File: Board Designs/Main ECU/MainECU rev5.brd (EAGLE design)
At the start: 120.6 x 78.9 mm, 164 parts, among them Q10 MMBT3904LT3G, Q11 MMBT3904LT3G, Q9 MMBT3904LT3G, X1 CONNECTOR-37, X2 CONNECTOR-4AUTOSPORT, X3 CONNECTOR-4NANO-FIT-VERTICAL-4, X4 CONNECTOR-4NANO-FIT-VERTICAL-4

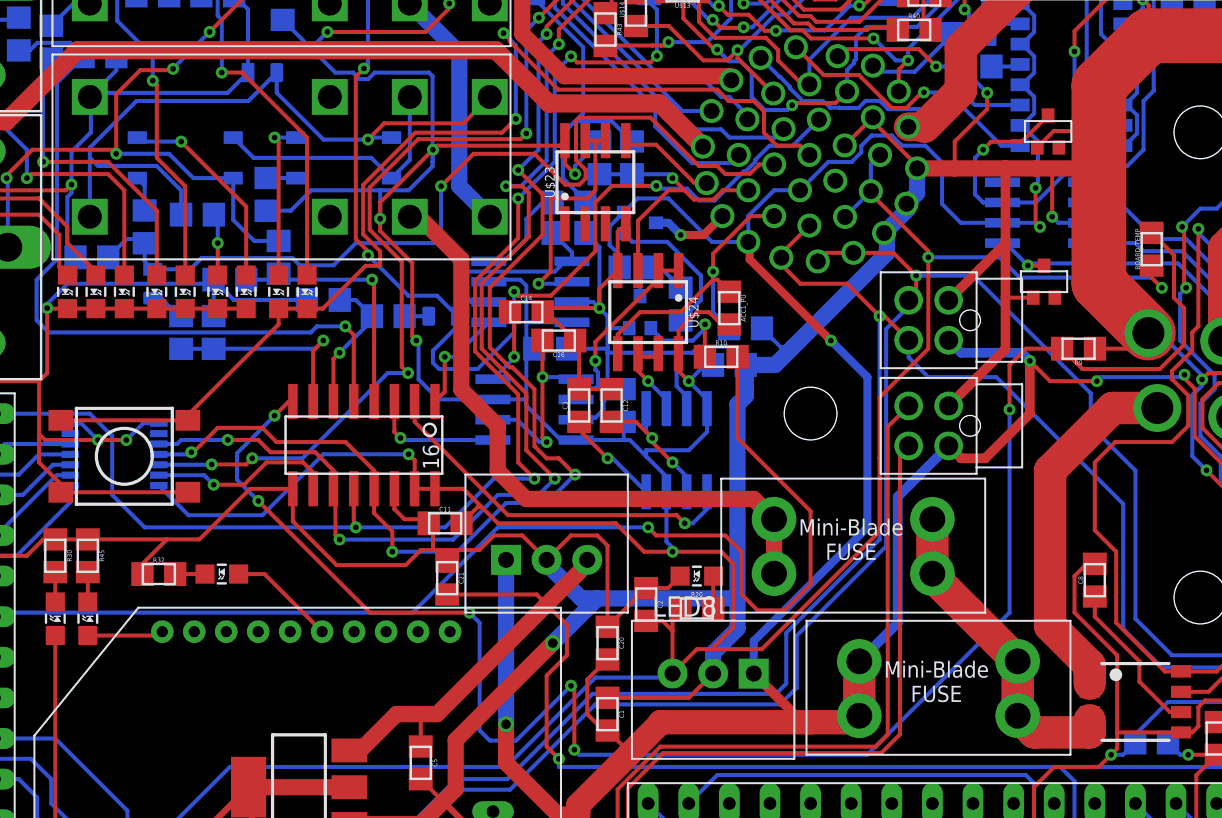
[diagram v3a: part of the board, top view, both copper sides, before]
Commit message: MainECU rev5: Added current sensor filter caps, fixed level shifter OE pin, various tweaks to traces
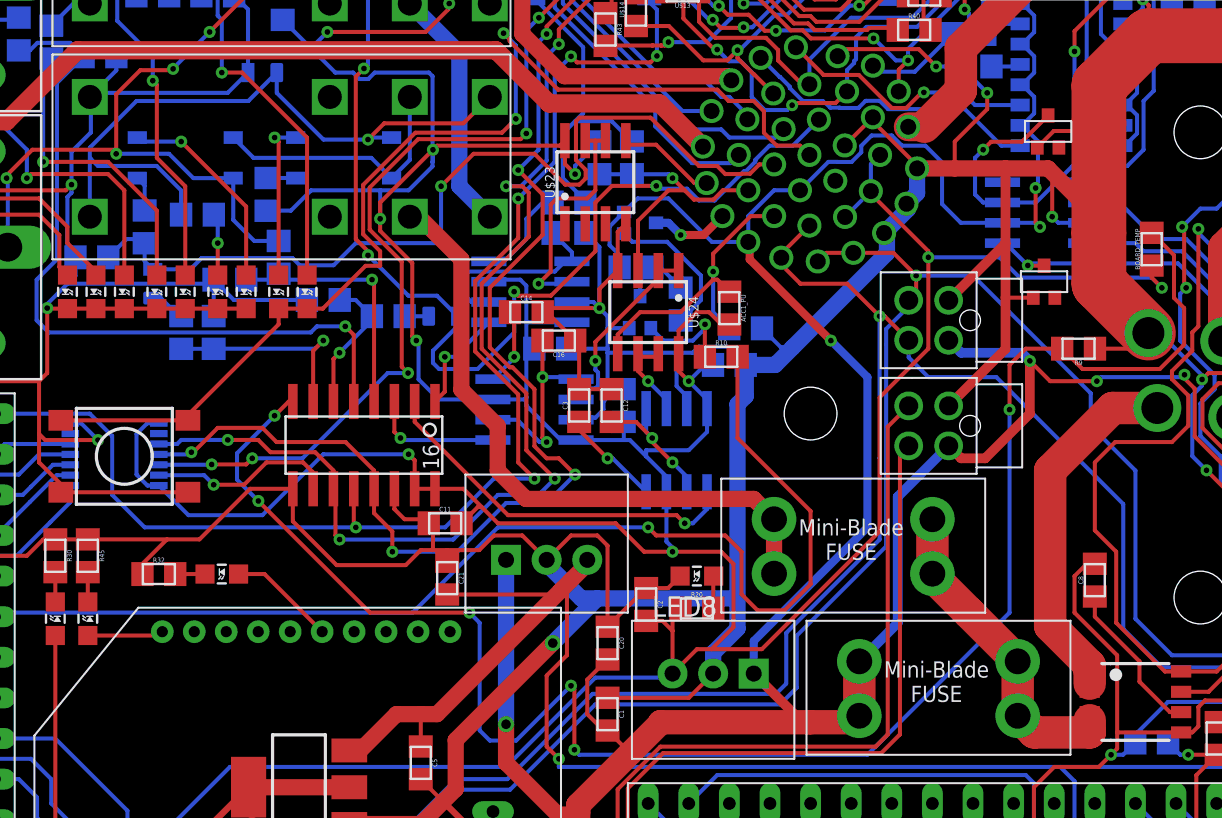
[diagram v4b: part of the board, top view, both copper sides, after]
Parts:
- C7, C8: value (none) -> 47nF
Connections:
- net +5V: now also U$25.8
- net GND: no longer U$25.8
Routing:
- net +5V: track 337.5 -> 343.4 mm
- net GND: track 852.2 -> 849.3 mm, vias 30 -> 29
- net TELEMETRY5V: track 299.0 -> 300.8 mm
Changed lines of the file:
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@@
 <layer number="25" name="tNames" color="7" fill="1" visible="yes" active="yes"/>
 <layer number="26" name="bNames" color="7" fill="1" visible="yes" active="yes"/>
-<layer number="27" name="tValues" color="7" fill="1" visible="yes" active="yes"/>
-<layer number="28" name="bValues" color="7" fill="1" visible="yes" active="yes"/>
+<layer number="27" name="tValues" color="7" fill="1" visible="no" active="yes"/>
+<layer number="28" name="bValues" color="7" fill="1" visible="no" active="yes"/>
 <layer number="29" name="tStop" color="7" fill="3" visible="no" active="yes"/>
 <layer number="30" name="bStop" color="7" fill="6" visible="no" active="yes"/>
@@
 <layer number="42" name="bRestrict" color="1" fill="10" visible="yes" active="yes"/>
 <layer number="43" name="vRestrict" color="2" fill="10" visible="no" active="yes"/>
-<layer number="44" name="Drills" color="7" fill="1" visible="yes" active="yes"/>
-<layer number="45" name="Holes" color="7" fill="1" visible="yes" active="yes"/>
+<layer number="44" name="Drills" color="7" fill="1" visible="no" active="yes"/>
+<layer number="45" name="Holes" color="7" fill="1" visible="no" active="yes"/>
 <layer number="46" name="Milling" color="3" fill="1" visible="no" active="yes"/>
 <layer number="47" name="Measures" color="7" fill="1" visible="no" active="yes"/>
@@
 <attribute name="VALUE" x="38.1" y="15.9512" size="0.3048" layer="27" rot="R180" align="top-center"/>
 </element>
-<element name="C7" library="HyTechDevices" package="0805" value="" x="95.504" y="66.294" smashed="yes" rot="MR0">
+<element name="C7" library="HyTechDevices" package="0805" value="47nF" x="95.504" y="66.294" smashed="yes" rot="MR0">
 <attribute name="NAME" x="95.504" y="67.0179" size="0.3048" layer="26" rot="MR0" align="bottom-center"/>
 <attribute name="VALUE" x="95.504" y="65.5828" size="0.3048" layer="28" rot="MR0" align="top-center"/>
 </element>
-<element name="C8" library="HyTechDevices" package="0805" value="" x="87.63" y="32.258" smashed="yes" rot="R90">
+<element name="C8" library="HyTechDevices" package="0805" value="47nF" x="87.63" y="32.258" smashed="yes" rot="R90">
 <attribute name="NAME" x="86.9061" y="32.258" size="0.3048" layer="25" rot="R90" align="bottom-center"/>
 <attribute name="VALUE" x="88.3412" y="32.258" size="0.3048" layer="27" rot="R90" align="top-center"/>
@@
 <wire x1="76.513353125" y1="56.467409375" x2="75.935971875" y2="55.890028125" width="1.016" layer="16"/>
 <wire x1="95.7072" y1="66.3092" x2="90.998" y2="66.3092" width="3.429" layer="1"/>
-<wire x1="87.884" y1="50.812765625" x2="87.884" y2="58.166" width="3.429" layer="1"/>
+<wire x1="87.884" y1="50.812765625" x2="87.884" y2="53.975" width="3.429" layer="1"/>
 <wire x1="87.884" y1="63.1952" x2="87.884" y2="60.833" width="3.429" layer="1"/>
-<wire x1="87.884" y1="60.833" x2="87.884" y2="58.166" width="3.429" layer="1"/>
 <wire x1="93.03" y1="22.733" x2="89.027" y2="22.733" width="0.254" layer="1"/>
 <wire x1="99.822" y1="28.448" x2="99.822" y2="25.527" width="0.254" layer="16"/>
@@
 <wire x1="76.513353125" y1="58.0120125" x2="78.867" y2="58.0120125" width="1.016" layer="1"/>
 <wire x1="78.867" y1="58.0120125" x2="82.042" y2="58.0120125" width="1.016" layer="1"/>
-<wire x1="82.042" y1="58.0120125" x2="83.947" y2="58.0120125" width="1.016" layer="1"/>
-<wire x1="83.947" y1="58.0120125" x2="87.7300125" y2="58.0120125" width="1.016" layer="1"/>
-<wire x1="87.7300125" y1="58.0120125" x2="87.884" y2="58.166" width="1.016" layer="1"/>
+<wire x1="82.042" y1="58.0120125" x2="84.709" y2="58.0120125" width="1.016" layer="1"/>
 <contactref element="Q9" pad="2"/>
 <via x="15.24" y="57.404" extent="1-16" drill="0.381"/>
@@
 <wire x1="9.271" y1="72.771" x2="9.271" y2="70.374" width="0.254" layer="16"/>
 <wire x1="22.987" y1="74.041" x2="10.541" y2="74.041" width="0.254" layer="1"/>
-<contactref element="U$25" pad="8"/>
-<wire x1="29.0798" y1="42.0745" x2="28.1045" y2="42.0745" width="0.254" layer="16"/>
-<wire x1="28.1045" y1="42.0745" x2="27.051" y2="41.021" width="0.254" layer="16"/>
-<via x="27.051" y="41.021" extent="1-16" drill="0.35"/>
 <contactref element="U$25" pad="7"/>
 <wire x1="23.5442" y1="42.0745" x2="24.2195" y2="42.0745" width="0.254" layer="16"/>
 <wire x1="24.2195" y1="42.0745" x2="25.273" y2="41.021" width="0.254" layer="16"/>
 <via x="25.273" y="41.021" extent="1-16" drill="0.35"/>
-<wire x1="25.273" y1="41.021" x2="27.051" y2="41.021" width="0.254" layer="1"/>
 <wire x1="21.59" y1="41.402" x2="21.971" y2="41.021" width="0.254" layer="1"/>
 <wire x1="21.971" y1="41.021" x2="25.273" y2="41.021" width="0.254" layer="1"/>
@@
 <via x="84.963" y="54.991" extent="1-16" drill="0.35"/>
 <wire x1="84.963" y1="54.991" x2="84.963" y2="58.0120125" width="0.254" layer="1"/>
-<wire x1="84.963" y1="58.0120125" x2="83.947" y2="58.0120125" width="0.254" layer="1"/>
+<wire x1="84.963" y1="58.0120125" x2="84.709" y2="58.0120125" width="0.254" layer="1"/>
 <wire x1="100.076" y1="48.251" x2="100.076" y2="48.133" width="0.254" layer="1"/>
 <via x="94.3384" y="44.8126125" extent="1-16" drill="0.35"/>
@@
 <wire x1="90.005534375" y1="46.736" x2="90.98315" y2="47.713615625" width="0.254" layer="1"/>
 <wire x1="94.615" y1="39.1266" x2="97.155" y2="36.5866" width="0.254" layer="1"/>
+<wire x1="84.709" y1="58.0120125" x2="87.884" y2="54.8370125" width="1.016" layer="1"/>
+<wire x1="87.884" y1="54.8370125" x2="87.884" y2="53.975" width="1.016" layer="1"/>
+<wire x1="87.884" y1="60.833" x2="87.884" y2="53.975" width="3.429" layer="1"/>
 </signal>
 <signal name="+12V">
@@
 <wire x1="82.931" y1="51.181" x2="91.186" y2="51.181" width="0.254" layer="16"/>
 <wire x1="91.186" y1="51.181" x2="91.821" y2="50.546" width="0.254" layer="16"/>
+<contactref element="U$25" pad="8"/>
+<wire x1="29.0798" y1="42.0745" x2="28.3585" y2="42.0745" width="0.254" layer="16"/>
+<wire x1="28.3585" y1="42.0745" x2="27.686" y2="41.402" width="0.254" layer="16"/>
+<wire x1="27.686" y1="41.402" x2="27.686" y2="38.862" width="0.254" layer="16"/>
+<wire x1="28.3735" y1="38.1745" x2="29.0798" y2="38.1745" width="0.254" layer="16"/>
+<wire x1="27.686" y1="38.862" x2="28.3735" y2="38.1745" width="0.254" layer="16"/>
 </signal>
 <signal name="IMD_PWR_STEP">
@@
 <wire x1="52.832" y1="50.8" x2="53.594" y2="51.562" width="0.254" layer="1"/>
 <wire x1="56.388" y1="59.75" x2="55.753" y2="59.75" width="0.254" layer="1"/>
-<wire x1="53.594" y1="56.134" x2="55.88" y2="56.134" width="0.254" layer="1"/>
-<wire x1="53.594" y1="51.562" x2="53.594" y2="56.134" width="0.254" layer="1"/>
+<wire x1="55.88" y1="56.134" x2="53.975" y2="56.134" width="0.254" layer="1"/>
+<wire x1="53.594" y1="55.753" x2="53.594" y2="51.562" width="0.254" layer="1"/>
 <wire x1="55.88" y1="56.134" x2="56.388" y2="56.642" width="0.254" layer="1"/>
+<wire x1="53.975" y1="56.134" x2="53.594" y2="55.753" width="0.254" layer="1"/>
 </signal>
 <signal name="OKHS_READ">
@@
 <contactref element="C21" pad="2"/>
 <contactref element="REG3" pad="3"/>
-<wire x1="55.88" y1="33.274" x2="53.34" y2="30.734" width="1.016" layer="1"/>
-<wire x1="53.34" y1="30.734" x2="46.482" y2="23.876" width="1.016" layer="1"/>
+<wire x1="55.88" y1="33.274" x2="54.864" y2="32.258" width="1.016" layer="1"/>
+<wire x1="54.864" y1="32.258" x2="54.229" y2="31.623" width="1.016" layer="1"/>
+<wire x1="54.229" y1="31.623" x2="46.482" y2="23.876" width="1.016" layer="1"/>
 <contactref element="CAN_TRANSCEIVER2" pad="3"/>
 <wire x1="118.11" y1="3.048" x2="115.824" y2="5.334" width="0.254" layer="1"/>
@@
 <wire x1="45.466" y1="23.876" x2="43.942" y2="23.876" width="1.016" layer="1"/>
 <wire x1="45.466" y1="21.853" x2="45.466" y2="23.876" width="0.254" layer="1"/>
-<wire x1="53.34" y1="30.734" x2="54.61" y2="29.464" width="0.254" layer="1"/>
-<wire x1="54.61" y1="29.464" x2="54.61" y2="27.559" width="0.254" layer="1"/>
 <wire x1="54.61" y1="27.559" x2="53.34" y2="26.289" width="0.254" layer="1"/>
-<wire x1="52.714" y1="31.36" x2="53.34" y2="30.734" width="0.254" layer="1"/>
-<wire x1="47.117" y1="31.36" x2="52.714" y2="31.36" width="0.254" layer="1"/>
+<wire x1="47.117" y1="31.36" x2="53.966" y2="31.36" width="0.254" layer="1"/>
 <wire x1="101.854" y1="62.992" x2="101.854" y2="52.324" width="0.254" layer="16"/>
 <wire x1="101.854" y1="52.324" x2="100.711" y2="51.181" width="0.254" layer="16"/>
@@
 <wire x1="92.456" y1="45.339" x2="93.726" y2="46.609" width="0.254" layer="1"/>
 <wire x1="93.726" y1="46.609" x2="93.726" y2="47.752" width="0.254" layer="1"/>
+<wire x1="53.966" y1="31.36" x2="54.229" y2="31.623" width="0.254" layer="1"/>
+<wire x1="54.61" y1="27.559" x2="54.61" y2="32.004" width="0.254" layer="1"/>
+<wire x1="54.61" y1="32.004" x2="54.864" y2="32.258" width="0.254" layer="1"/>
 </signal>
 <signal name="VCC">

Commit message: Main ECU rev{1-5}: Update values of LED resistors based on testing
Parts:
- LED7: value Green -> 20k
- R11: value 43 -> 150
- R14, R21: value 820 -> 2k
- R16, R25, R32, R51, R52: value 100 -> 1.2k
- R31: value 1.2K -> 6.8k
- R45: value 33 -> 0
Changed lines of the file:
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@@
 <element name="LED3" library="HyTechDevices" package="LED-805" value="Green" x="30.734" y="50.292" smashed="yes" rot="R180"/>
 <element name="LED5" library="HyTechDevices" package="LED-805" value="Yellow" x="32.766" y="50.292" smashed="yes" rot="R180"/>
-<element name="LED7" library="HyTechDevices" package="LED-805" value="Green" x="28.956" y="50.292" smashed="yes" rot="R180"/>
+<element name="LED7" library="HyTechDevices" package="LED-805" value="20k" x="28.956" y="50.292" smashed="yes" rot="R180"/>
 <element name="LED8" library="HyTechDevices" package="LED-805" value="Purple" x="62.738" y="32.512" smashed="yes" rot="R90">
 <attribute name="NAME" x="64.008" y="31.242" size="1.27" layer="25" ratio="10" rot="R180"/>
@@
 <attribute name="VALUE" x="94.5388" y="22.352" size="0.3048" layer="27" rot="R270" align="top-center"/>
 </element>
-<element name="R11" library="HyTechDevices" package="0805" value="43" x="28.702" y="68.834" smashed="yes" rot="MR180">
+<element name="R11" library="HyTechDevices" package="0805" value="150" x="28.702" y="68.834" smashed="yes" rot="MR180">
 <attribute name="NAME" x="28.702" y="68.1101" size="0.3048" layer="26" rot="MR180" align="bottom-center"/>
 <attribute name="VALUE" x="28.702" y="69.5452" size="0.3048" layer="28" rot="MR180" align="top-center"/>
@@
 <attribute name="VALUE" x="36.1188" y="68.326" size="0.3048" layer="28" rot="MR90" align="top-center"/>
 </element>
-<element name="R14" library="HyTechDevices" package="0805" value="820" x="31.496" y="55.118" smashed="yes" rot="MR180">
+<element name="R14" library="HyTechDevices" package="0805" value="2k" x="31.496" y="55.118" smashed="yes" rot="MR180">
 <attribute name="NAME" x="31.496" y="54.3941" size="0.3048" layer="26" rot="MR180" align="bottom-center"/>
 <attribute name="VALUE" x="31.496" y="55.8292" size="0.3048" layer="28" rot="MR180" align="top-center"/>
@@
 <attribute name="VALUE" x="62.738" y="29.7688" size="0.3048" layer="27" align="top-center"/>
 </element>
-<element name="R21" library="HyTechDevices" package="0805" value="820" x="28.194" y="54.356" smashed="yes" rot="MR90">
+<element name="R21" library="HyTechDevices" package="0805" value="2k" x="28.194" y="54.356" smashed="yes" rot="MR90">
 <attribute name="NAME" x="28.9179" y="54.356" size="0.3048" layer="26" rot="MR90" align="bottom-center"/>
 <attribute name="VALUE" x="27.4828" y="54.356" size="0.3048" layer="28" rot="MR90" align="top-center"/>
@@
 <attribute name="VALUE" x="21.8948" y="33.782" size="0.3048" layer="27" rot="R270" align="top-center"/>
 </element>
-<element name="R31" library="HyTechDevices" package="0805" value="1.2K" x="11.811" y="58.674" smashed="yes" rot="MR270">
+<element name="R31" library="HyTechDevices" package="0805" value="6.8k" x="11.811" y="58.674" smashed="yes" rot="MR270">
 <attribute name="NAME" x="11.0871" y="58.674" size="0.3048" layer="26" rot="MR270" align="bottom-center" display="off"/>
 <attribute name="VALUE" x="12.5222" y="58.674" size="0.3048" layer="28" rot="MR270" align="top-center" display="off"/>
 </element>
-<element name="R32" library="HyTechDevices" package="0805" value="100" x="29.083" y="32.639" smashed="yes">
+<element name="R32" library="HyTechDevices" package="0805" value="1.2k" x="29.083" y="32.639" smashed="yes">
 <attribute name="NAME" x="29.083" y="33.3629" size="0.3048" layer="25" align="bottom-center"/>
 <attribute name="VALUE" x="29.083" y="31.9278" size="0.3048" layer="27" align="top-center"/>
@@
 <attribute name="VALUE" x="79.756" y="65.7098" size="0.3048" layer="28" rot="MR0" align="top-center"/>
 </element>
-<element name="R45" library="HyTechDevices" package="0805" value="33" x="24.638" y="33.782" smashed="yes" rot="R270">
+<element name="R45" library="HyTechDevices" package="0805" value="0" x="24.638" y="33.782" smashed="yes" rot="R270">
 <attribute name="NAME" x="25.3619" y="33.782" size="0.3048" layer="25" rot="R270" align="bottom-center"/>
 <attribute name="VALUE" x="23.9268" y="33.782" size="0.3048" layer="27" rot="R270" align="top-center"/>
@@
 <element name="U$8" library="HyTechDevices" package="ZF112" value="G5LE" x="21.59" y="61.976" smashed="yes" rot="R180"/>
 <element name="LED6" library="HyTechDevices" package="LED-805" value="Red" x="23.368" y="50.292" smashed="yes" rot="R180"/>
-<element name="R16" library="HyTechDevices" package="0805" value="100" x="4.572" y="54.356" smashed="yes" rot="MR270">
+<element name="R16" library="HyTechDevices" package="0805" value="1.2k" x="4.572" y="54.356" smashed="yes" rot="MR270">
 <attribute name="NAME" x="3.8481" y="54.356" size="0.3048" layer="26" rot="MR270" align="bottom-center" display="off"/>
 <attribute name="VALUE" x="5.2832" y="54.356" size="0.3048" layer="28" rot="MR270" align="top-center" display="off"/>
@@
 <attribute name="VALUE" x="106.934" y="61.468" size="1.27" layer="27" ratio="10"/>
 </element>
-<element name="R25" library="HyTechDevices" package="0805" value="100" x="108.331" y="63.754" smashed="yes" rot="MR0">
+<element name="R25" library="HyTechDevices" package="0805" value="1.2k" x="108.331" y="63.754" smashed="yes" rot="MR0">
 <attribute name="NAME" x="108.331" y="64.4779" size="0.3048" layer="26" rot="MR0" align="bottom-center"/>
 <attribute name="VALUE" x="108.331" y="63.0428" size="0.3048" layer="28" rot="MR0" align="top-center"/>
@@
 <attribute name="VALUE" x="116.586" y="31.496" size="1.27" layer="27" ratio="10"/>
 </element>
-<element name="R51" library="HyTechDevices" package="0805" value="100" x="117.856" y="31.877" smashed="yes" rot="R180">
+<element name="R51" library="HyTechDevices" package="0805" value="1.2k" x="117.856" y="31.877" smashed="yes" rot="R180">
 <attribute name="NAME" x="117.856" y="31.1531" size="0.3048" layer="25" rot="R180" align="bottom-center"/>
 <attribute name="VALUE" x="117.856" y="32.5882" size="0.3048" layer="27" rot="R180" align="top-center"/>
@@
 <attribute name="VALUE" x="115.316" y="60.325" size="1.27" layer="27" ratio="10"/>
 </element>
-<element name="R52" library="HyTechDevices" package="0805" value="100" x="116.586" y="62.992" smashed="yes" rot="MR0">
+<element name="R52" library="HyTechDevices" package="0805" value="1.2k" x="116.586" y="62.992" smashed="yes" rot="MR0">
 <attribute name="NAME" x="116.586" y="63.7159" size="0.3048" layer="26" rot="MR0" align="bottom-center"/>
 <attribute name="VALUE" x="116.586" y="62.2808" size="0.3048" layer="28" rot="MR0" align="top-center"/>

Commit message: Main ECU rev{1-5}: Update values of OKI-78SR capacitors to 10uF
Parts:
- C1, C20: value .22uF -> 10uF
- C2, C21: value .1uF -> 10uF
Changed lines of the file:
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@@
 <attribute name="VALUE" x="91.8972" y="52.959" size="0.3048" layer="27" rot="R90" align="top-center"/>
 </element>
-<element name="C1" library="HyTechDevices" package="0805" value=".22uF" x="57.15" y="23.876" smashed="yes" rot="R270">
+<element name="C1" library="HyTechDevices" package="0805" value="10uF" x="57.15" y="23.876" smashed="yes" rot="R270">
 <attribute name="NAME" x="57.8739" y="23.876" size="0.3048" layer="25" rot="R270" align="bottom-center"/>
 <attribute name="VALUE" x="56.4388" y="23.876" size="0.3048" layer="27" rot="R270" align="top-center"/>
@@
 <attribute name="VALUE" x="99.822" y="66.0908" size="0.3048" layer="28" rot="MR0" align="top-center"/>
 </element>
-<element name="C2" library="HyTechDevices" package="0805" value=".1uF" x="59.563" y="30.734" smashed="yes" rot="R270">
+<element name="C2" library="HyTechDevices" package="0805" value="10uF" x="59.563" y="30.734" smashed="yes" rot="R270">
 <attribute name="NAME" x="60.2869" y="30.734" size="0.3048" layer="25" rot="R270" align="bottom-center"/>
 <attribute name="VALUE" x="58.8518" y="30.734" size="0.3048" layer="27" rot="R270" align="top-center"/>
@@
 <element name="U$16" library="HyTechDevices" package="CR-2450/G1AN" value="CR-2450/G1AN" x="62.6872" y="12.7" smashed="yes" rot="MR270"/>
 <element name="REG3" library="HyTechDevices" package="OKI-78SR" value="5V" x="53.34" y="33.528" smashed="yes"/>
-<element name="C20" library="HyTechDevices" package="0805" value=".22uF" x="57.15" y="28.321" smashed="yes" rot="R270">
+<element name="C20" library="HyTechDevices" package="0805" value="10uF" x="57.15" y="28.321" smashed="yes" rot="R270">
 <attribute name="NAME" x="57.8739" y="28.321" size="0.3048" layer="25" rot="R270" align="bottom-center"/>
 <attribute name="VALUE" x="56.4388" y="28.321" size="0.3048" layer="27" rot="R270" align="top-center"/>
 </element>
-<element name="C21" library="HyTechDevices" package="0805" value=".1uF" x="47.117" y="32.385" smashed="yes" rot="R270">
+<element name="C21" library="HyTechDevices" package="0805" value="10uF" x="47.117" y="32.385" smashed="yes" rot="R270">
 <attribute name="NAME" x="47.8409" y="32.385" size="0.3048" layer="25" rot="R270" align="bottom-center"/>
 <attribute name="VALUE" x="46.4058" y="32.385" size="0.3048" layer="27" rot="R270" align="top-center"/>
